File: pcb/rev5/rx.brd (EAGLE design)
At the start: 19 x 38 mm, 34 parts, among them IC1 STM32F042F4, IC2 NRF24L01ALT1, SW1 SW_3POS_DEVSW_3POS_OFFICIAL, SW2 324_SW324_SWITCH_FOOT_HOLE, U1 USBC_16P, U2 XC6206_DEV, Y1 16MHz_12pF

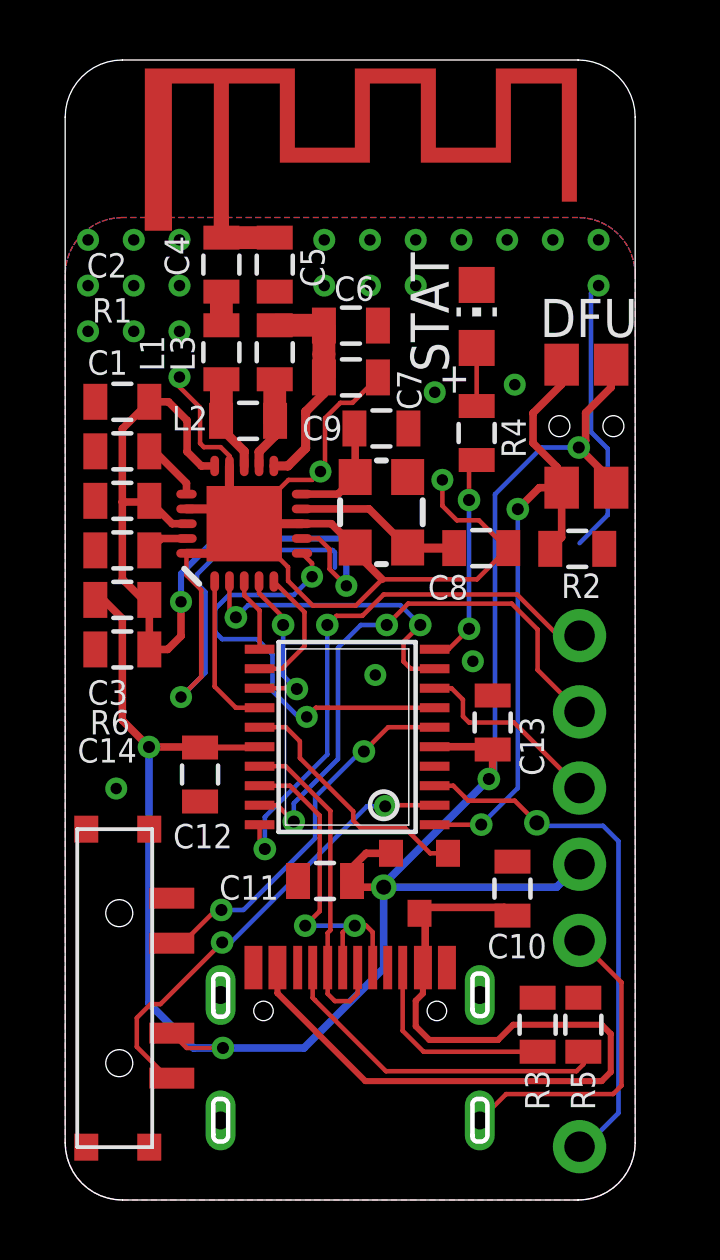
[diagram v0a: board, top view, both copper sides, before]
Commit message: added trig_out on RX, preparing for next production run
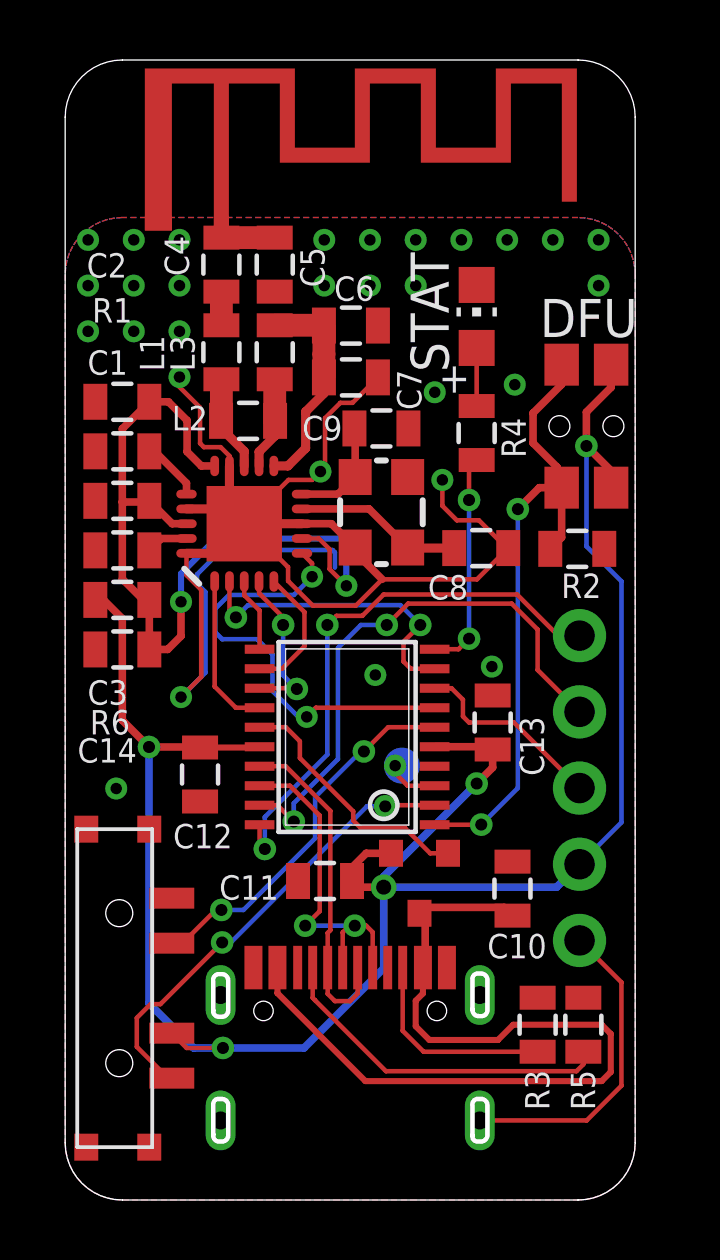
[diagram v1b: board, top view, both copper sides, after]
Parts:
- removed JP1: (no value), adafruit_changed:1X01-CLEANBIG
- added TP2: TPTP12R, testpad:TP12R
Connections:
- net N$19: now also TP2.TP; no longer JP1.1
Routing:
- net N$19: track 17.7 -> 1.74 mm
- net GND: track 81.6 -> 72.3 mm
- net +3V3: track 68.7 -> 70.0 mm
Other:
- board text added: "PD2 190823"
- board text added: "PF1"
- board text removed: "PD3 191005"
- board text removed: "TRIG"
